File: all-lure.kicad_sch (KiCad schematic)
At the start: 95 parts, among them J1 XDP, J2 mSATA, J3 mPCIe, J4 HSE, J5 Conn_01x02, J6 GPIO, J8 0480995701, J9 0480995701, U1 SC189HSKTRT, U2 SC189ZSKTRT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

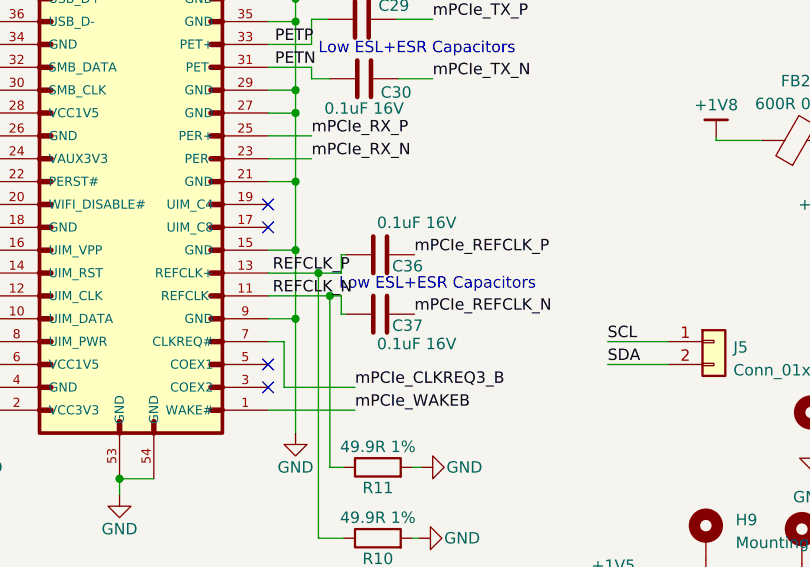
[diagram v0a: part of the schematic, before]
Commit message: feat(pcb): update with latest attempt at mSATA and mPCIE
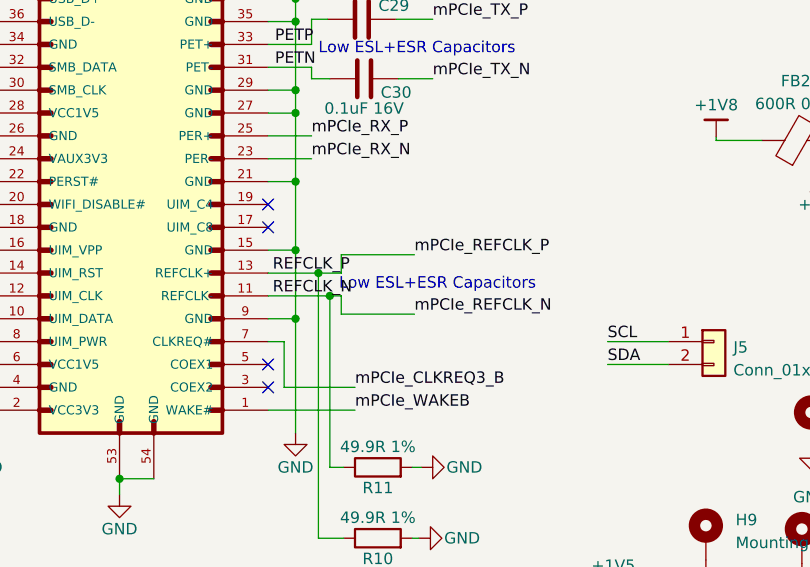
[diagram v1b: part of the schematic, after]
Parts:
- removed C36, C37: 0.1uF 16V, Capacitor_SMD:C_0402_1005Metric_Pad0.74x0.62mm_HandSolder, symbol Device:C
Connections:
- net mPCIe_REFCLK_N is gone; now on net REFCLK_N: J4.11 (mPCIe_REFCLK_N)
- net mPCIe_REFCLK_P is gone; now on net REFCLK_P: J4.9 (mPCIe_REFCLK_P)
